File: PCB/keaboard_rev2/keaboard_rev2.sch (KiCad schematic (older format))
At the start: 80 parts, among them K01 KEYSW, K02 KEYSW, K03 KEYSW, K04 KEYSW, K05 KEYSW, K06 KEYSW, K07 KEYSW, K08 KEYSW, K09 KEYSW, K10 KEYSW, K11 KEYSW, K12 KEYSW, K13 KEYSW, K14 KEYSW, K15 KEYSW, K16 KEYSW, K17 KEYSW, K18 KEYSW, K19 KEYSW, K20 KEYSW, K21 KEYSW, K22 KEYSW, K23 KEYSW, K24 KEYSW, K25 KEYSW, U1 ProMicro

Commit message: WIP rev2
Just traces remaining
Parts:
- removed D01, D02, D03, D04, D05, D06, D07, D08, D09, D10, D11, D12, D13, D14, D15, D16, D17, D18, D19, D20, D21, D22, D23, D24, D25: D, parts:D_SOD123_reversible, symbol keyboard_parts:D
- removed K01, K02, K03, K04, K05, K06, K07, K08, K09, K10, K11, K12, K13, K14, K15, K16, K17, K18, K19, K20, K21, K22, K23, K24, K25: KEYSW, parts:Kailh_socket_MX_reversible, symbol keyboard_parts:KEYSW
- removed LED01, LED02, LED03, LED04, LED05, LED06, LED07, LED08, LED09, LED10, LED11, LED12, LED13, LED14, LED15, LED16, LED17, LED18, LED19, LED20, LED21, LED22, LED23, LED24, LED25: WS2812B, LED_SMD:LED_WS2812B_PLCC4_5.0x5.0mm_P3.2mm, symbol LED:WS2812B
- removed R01: R2.2k, symbol Device:R
- removed R02: R10k, symbol Device:R
- removed SW_RST1: SW_EVQ-9P701P, parts:SW_EVQ-9P701P_reversible, symbol Switch:SW_MEC_5G
- removed TRRS1: TRRS Jack, parts:TRRS-PJ-320A_reversible, symbol keaboard_rev2-rescue:AudioPlug4-Connector-keaboard_rev1-rescue
- added D1, D10, D11, D12, D13, D14, D15, D16, D17, D18, D19, D2, D20, D21, D22, D23, D24, D25, D3, D4, D5, D6, D7, D8, D9: 1N4148W, parts:D_SOD123_reversible, symbol Diode:1N4148W
- added J1: AudioJack4, parts:TRRS-PJ-320A_reversible, symbol Connector:AudioJack4
- added LED1, LED10, LED11, LED12, LED13, LED14, LED15, LED16, LED17, LED18, LED19, LED2, LED20, LED21, LED22, LED23, LED24, LED25, LED3, LED4, LED5, LED6, LED7, LED8, LED9: SK6812MINI, parts:YS-SK6812MINI-E_reversible, symbol LED:SK6812MINI
- added RESET1: SW_Push, parts:SW_EVQ-9P701P_reversible, symbol Switch:SW_Push
- added SW1, SW10, SW11, SW12, SW13, SW14, SW15, SW16, SW17, SW18, SW19, SW2, SW20, SW21, SW22, SW23, SW24, SW25, SW3, SW4, SW5, SW6, SW7, SW8, SW9: SW_Push, keyswitches:Kailh_socket_PG1350_reversible, symbol Switch:SW_Push
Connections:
- net GND: now also J1.S, LED1.4 (VDD), LED10.4 (VDD), LED11.4 (VDD), LED12.4 (VDD), LED13.4 (VDD), LED14.4 (VDD), LED15.4 (VDD), LED16.4 (VDD), LED17.4 (VDD), LED18.4 (VDD), LED19.4 (VDD), LED2.4 (VDD), LED20.4 (VDD), LED21.4 (VDD), LED22.4 (VDD), LED23.4 (VDD), LED24.4 (VDD), LED25.4 (VDD), LED3.4 (VDD), LED4.4 (VDD), LED5.4 (VDD), LED6.4 (VDD), LED7.4 (VDD), LED8.4 (VDD), LED9.4 (VDD), RESET1.2
- net LED: now also U1.20 (F4), LED1.3 (DIN); no longer U1.1 (TX)
- net RAW: now also LED1.2 (VSS), LED10.2 (VSS), LED11.2 (VSS), LED12.2 (VSS), LED13.2 (VSS), LED14.2 (VSS), LED15.2 (VSS), LED16.2 (VSS), LED17.2 (VSS), LED18.2 (VSS), LED19.2 (VSS), LED2.2 (VSS), LED20.2 (VSS), LED21.2 (VSS), LED22.2 (VSS), LED23.2 (VSS), LED24.2 (VSS), LED25.2 (VSS), LED3.2 (VSS), LED4.2 (VSS), LED5.2 (VSS), LED6.2 (VSS), LED7.2 (VSS), LED8.2 (VSS), LED9.2 (VSS)
- net RESET: now also RESET1.1
- net Row1: now reaches U1.8 (C6)
- net Row1: now also D1.1 (K), D13.1 (K), D17.1 (K), D21.1 (K), D5.1 (K), D9.1 (K)
- net COL1 renamed TRRS_T
- net TRRS_T: now also J1.T
- net COL2 renamed Col7
- net Col7: now also SW24.2, SW25.2
- net COL3 renamed Col6
- net Col6: now also SW21.2, SW22.2, SW23.2
- net COL4 renamed Col5
- net Col5: now also SW17.2, SW18.2, SW19.2, SW20.2
- net COL5 renamed Col4
- net Col4: now also SW13.2, SW14.2, SW15.2, SW16.2
- net COL6 renamed Col3
- net Col3: now also SW10.2, SW11.2, SW12.2, SW9.2
- net COL7 renamed Col2
- net Col2: now also SW5.2, SW6.2, SW7.2, SW8.2
- net ROW1 renamed Row2
- net Row2: now also D10.1 (K), D14.1 (K), D18.1 (K), D2.1 (K), D22.1 (K), D6.1 (K)
- net ROW2 renamed Row3
- net Row3: now also D11.1 (K), D15.1 (K), D19.1 (K), D23.1 (K), D24.1 (K), D3.1 (K), D7.1 (K)
- net ROW3 renamed Row4
- net Row4: now also D12.1 (K), D16.1 (K), D20.1 (K), D25.1 (K), D4.1 (K), D8.1 (K)
- net ROW4 renamed Col1
- net Col1: now also SW1.2, SW2.2, SW3.2, SW4.2
- net SCL renamed TRRS_R2
- net TRRS_R2: now also J1.R2
- net SDA: no longer names the net of U1.6 (SDA)
- net VCC: no longer names the net of U1.21 (VCC)
- new net: LED1.1 (DOUT), LED2.3 (DIN)
- new net: D1.2 (A), SW1.1
- new net: D5.2 (A), SW5.1
- new net: D9.2 (A), SW9.1
- new net: D13.2 (A), SW13.1
- new net: D17.2 (A), SW17.1
- new net: D21.2 (A), SW21.1
- new net: D22.2 (A), SW22.1
- new net: D18.2 (A), SW18.1
- new net: D14.2 (A), SW14.1
- new net: D10.2 (A), SW10.1
- new net: D6.2 (A), SW6.1
- new net: D2.2 (A), SW2.1
- new net: D3.2 (A), SW3.1
- new net: D7.2 (A), SW7.1
- new net: D11.2 (A), SW11.1
- new net: D15.2 (A), SW15.1
- new net: D19.2 (A), SW19.1
- new net: D23.2 (A), SW23.1
- new net: D24.2 (A), SW24.1
- new net: D25.2 (A), SW25.1
- new net: D20.2 (A), SW20.1
- new net: D16.2 (A), SW16.1
- new net: D12.2 (A), SW12.1
- new net: D8.2 (A), SW8.1
- new net: D4.2 (A), SW4.1
- new net: LED2.1 (DOUT), LED3.3 (DIN)
- new net: LED3.1 (DOUT), LED4.3 (DIN)
- new net: LED4.1 (DOUT), LED5.3 (DIN)
- new net: LED5.1 (DOUT), LED6.3 (DIN)
- new net: LED6.1 (DOUT), LED7.3 (DIN)
- new net: LED7.1 (DOUT), LED8.3 (DIN)
- new net: LED8.1 (DOUT), LED9.3 (DIN)
- new net: LED10.3 (DIN), LED9.1 (DOUT)
- new net: LED10.1 (DOUT), LED11.3 (DIN)
- new net: LED11.1 (DOUT), LED12.3 (DIN)
- new net: LED12.1 (DOUT), LED13.3 (DIN)
- new net: LED13.1 (DOUT), LED14.3 (DIN)
- new net: LED14.1 (DOUT), LED15.3 (DIN)
- new net: LED15.1 (DOUT), LED16.3 (DIN)
- new net: LED16.1 (DOUT), LED17.3 (DIN)
- new net: LED17.1 (DOUT), LED18.3 (DIN)
- new net: LED18.1 (DOUT), LED19.3 (DIN)
- new net: LED19.1 (DOUT), LED20.3 (DIN)
- new net: LED20.1 (DOUT), LED21.3 (DIN)
- new net: LED21.1 (DOUT), LED22.3 (DIN)
- new net: LED22.1 (DOUT), LED23.3 (DIN)
- new net: LED23.1 (DOUT), LED24.3 (DIN)
- new net: LED24.1 (DOUT), LED25.3 (DIN)
- no-connect marks 6 -> 7

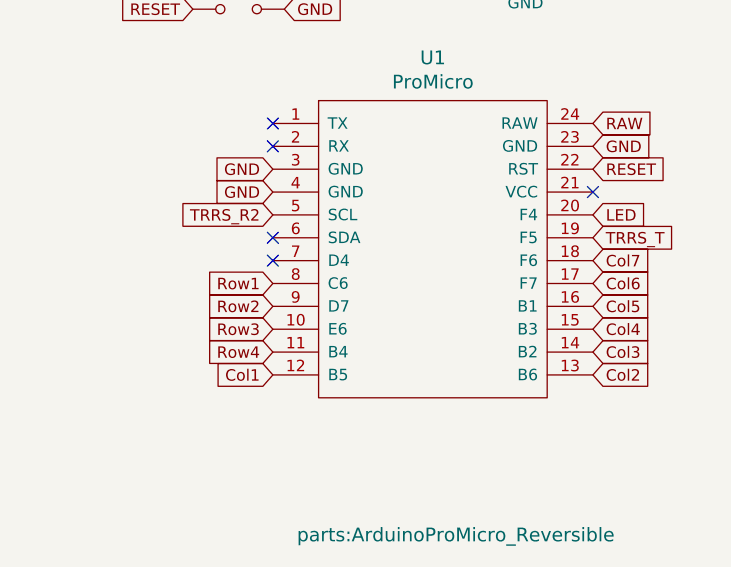
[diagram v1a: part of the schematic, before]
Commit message: Fix schematic/net mistake from old rev1 pdf
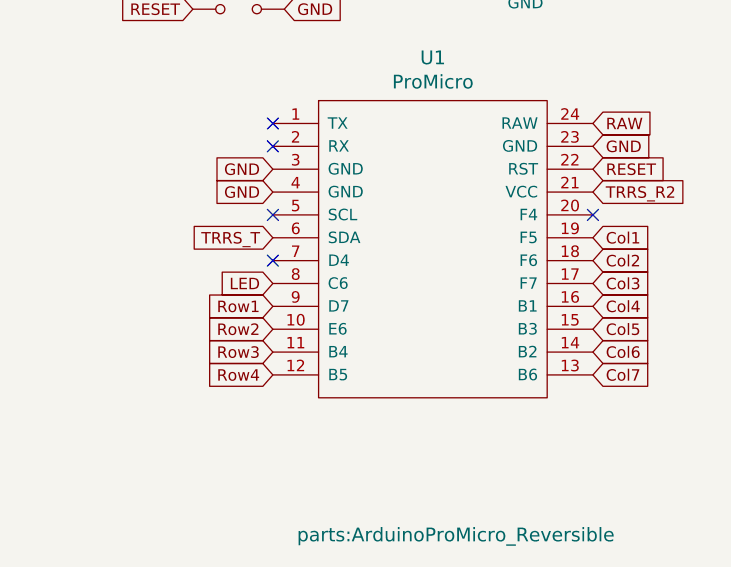
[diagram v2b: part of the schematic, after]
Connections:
- net Col1: now also U1.19 (F5); no longer U1.12 (B5)
- net Col2: now also U1.18 (F6); no longer U1.13 (B6)
- net Col3: now also U1.17 (F7); no longer U1.14 (B2)
- net Col4: now also U1.16 (B1); no longer U1.15 (B3)
- net Col5: now also U1.15 (B3); no longer U1.16 (B1)
- net Col6: now also U1.14 (B2); no longer U1.17 (F7)
- net Col7: now also U1.13 (B6); no longer U1.18 (F6)
- net LED: now also U1.8 (C6); no longer U1.20 (F4)
- net Row1: now also U1.9 (D7); no longer U1.8 (C6)
- net Row2: now also U1.10 (E6); no longer U1.9 (D7)
- net Row3: now also U1.11 (B4); no longer U1.10 (E6)
- net Row4: now also U1.12 (B5); no longer U1.11 (B4)
- net TRRS_R2: now also U1.21 (VCC); no longer U1.5 (SCL)
- net TRRS_T: now also U1.6 (SDA); no longer U1.19 (F5)
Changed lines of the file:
@@
 Text GLabel 6250 3300 1    50   Input ~ 0
 Col6
+Text GLabel 10600 5550 2    50   Input ~ 0
+Col2
+Text GLabel 10600 5650 2    50   Input ~ 0
+Col3
+Text GLabel 10600 5750 2    50   Input ~ 0
+Col4
+Text GLabel 10600 5850 2    50   Input ~ 0
+Col5
+Text GLabel 10600 5950 2    50   Input ~ 0
+Col6
+Text GLabel 9200 5750 0    50   Input ~ 0
+Row1
+Text GLabel 9200 5850 0    50   Input ~ 0
+Row2
+Text GLabel 9200 5950 0    50   Input ~ 0
+Row3
 Text GLabel 9200 6050 0    50   Input ~ 0
-Col1
-Text GLabel 10600 6050 2    50   Input ~ 0
-Col2
-Text GLabel 10600 5950 2    50   Input ~ 0
-Col3
-Text GLabel 10600 5850 2    50   Input ~ 0
-Col4
-Text GLabel 10600 5750 2    50   Input ~ 0
-Col5
-Text GLabel 10600 5650 2    50   Input ~ 0
-Col6
-Text GLabel 9200 5650 0    50   Input ~ 0
-Row1
-Text GLabel 9200 5750 0    50   Input ~ 0
-Row2
-Text GLabel 9200 5850 0    50   Input ~ 0
-Row3
-Text GLabel 9200 5950 0    50   Input ~ 0
 Row4
 Text GLabel 7150 3300 1    50   Input ~ 0
@@
 GND
 NoConn ~ 10100 3700
-Text GLabel 10600 5450 2    50   Input ~ 0
-TRRS_T
-Text GLabel 9200 5350 0    50   Input ~ 0
-TRRS_R2
 Text GLabel 10200 4250 0    50   Input ~ 0
 GND
@@
 Text GLabel 1200 1450 0    50   Input ~ 0
 RAW
-Text GLabel 10600 5350 2    50   Input ~ 0
+Text GLabel 9200 5650 0    50   Input ~ 0
 LED
-NoConn ~ 10600 5250
 NoConn ~ 9200 4950
 NoConn ~ 9200 5050
-NoConn ~ 9200 5450
 NoConn ~ 9200 5550
 Wire Wire Line
@@
 Wire Wire Line
 	6250 3300 6250 3450
-Text GLabel 10600 5550 2    50   Input ~ 0
+Text GLabel 10600 6050 2    50   Input ~ 0
 Col7
 Connection ~ 1850 1450
@@
 Wire Wire Line
 	10250 2300 10650 2300
+Text GLabel 10600 5250 2    50   Input ~ 0
+TRRS_R2
+Text GLabel 9200 5450 0    50   Input ~ 0
+TRRS_T
+Text GLabel 10600 5450 2    50   Input ~ 0
+Col1
+NoConn ~ 10600 5350
+NoConn ~ 9200 5350
 $EndSCHEMATC

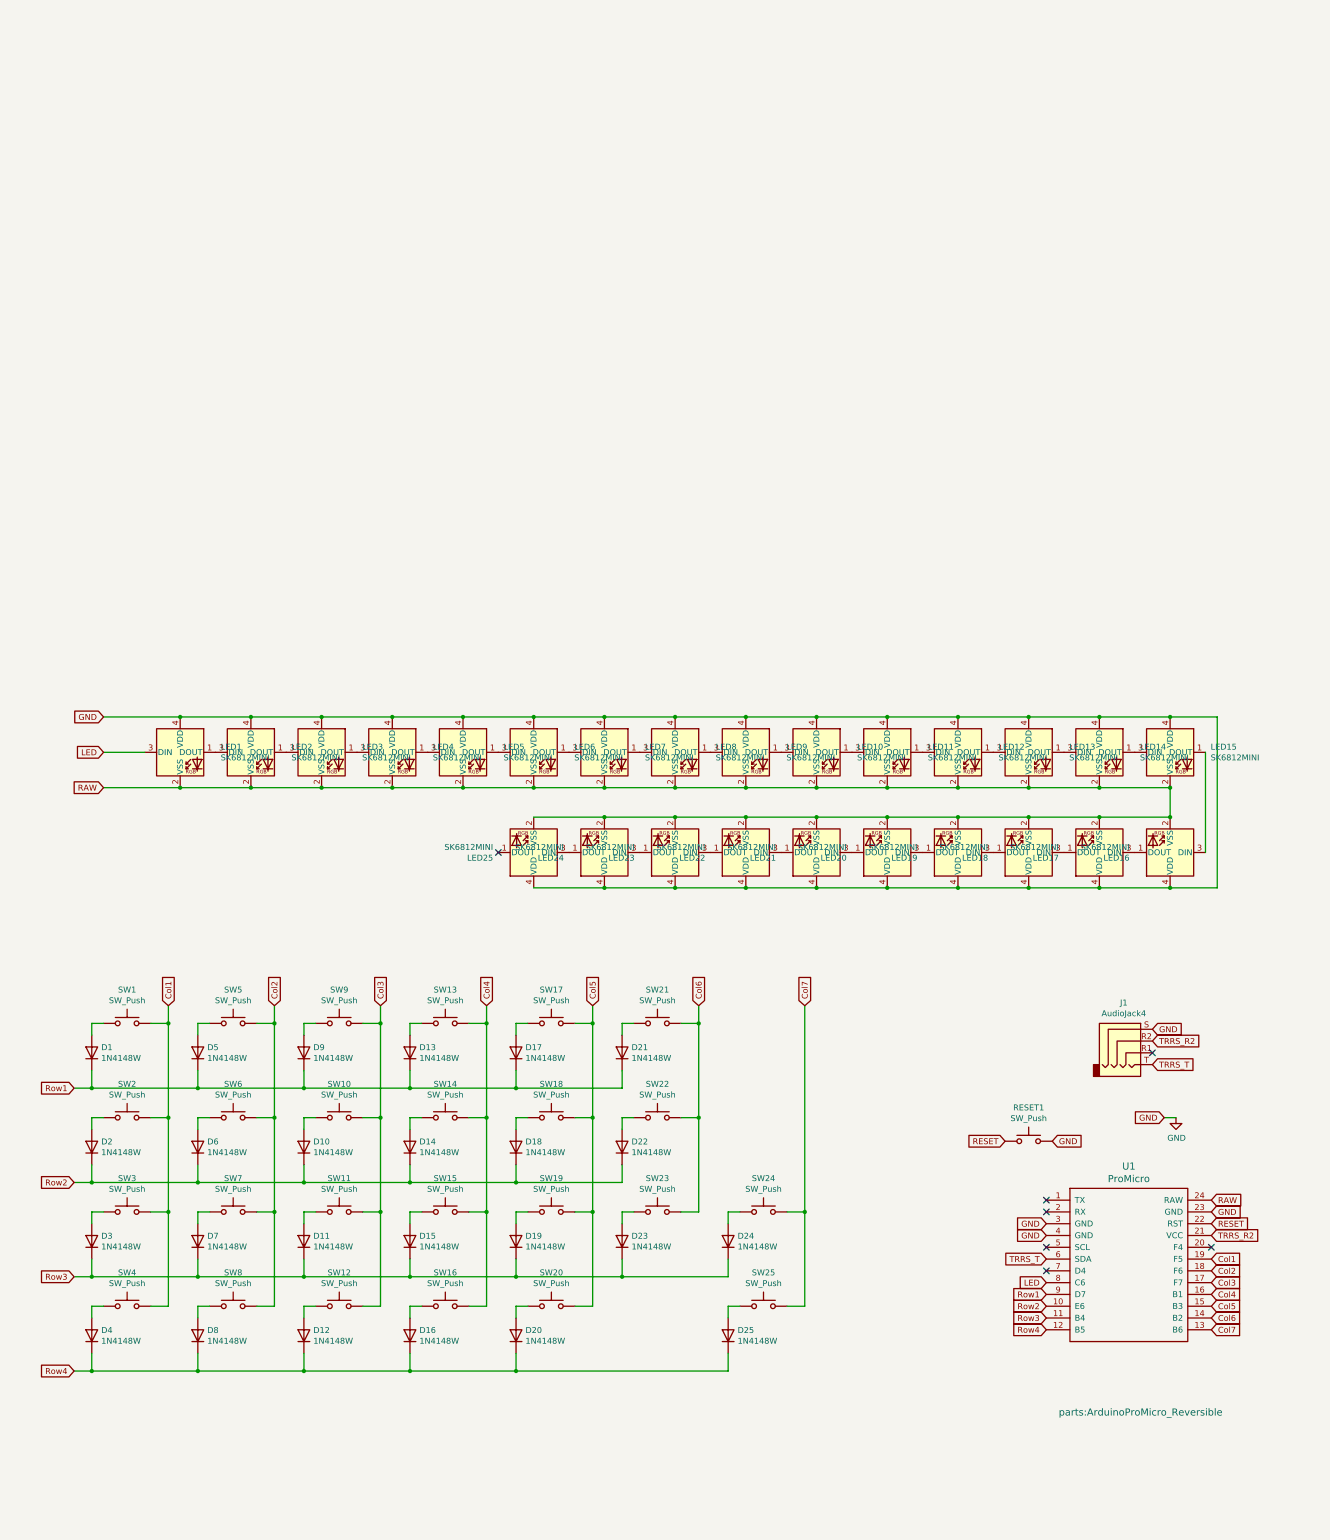
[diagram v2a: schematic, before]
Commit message: Reorder LEDs in schematic for better routing
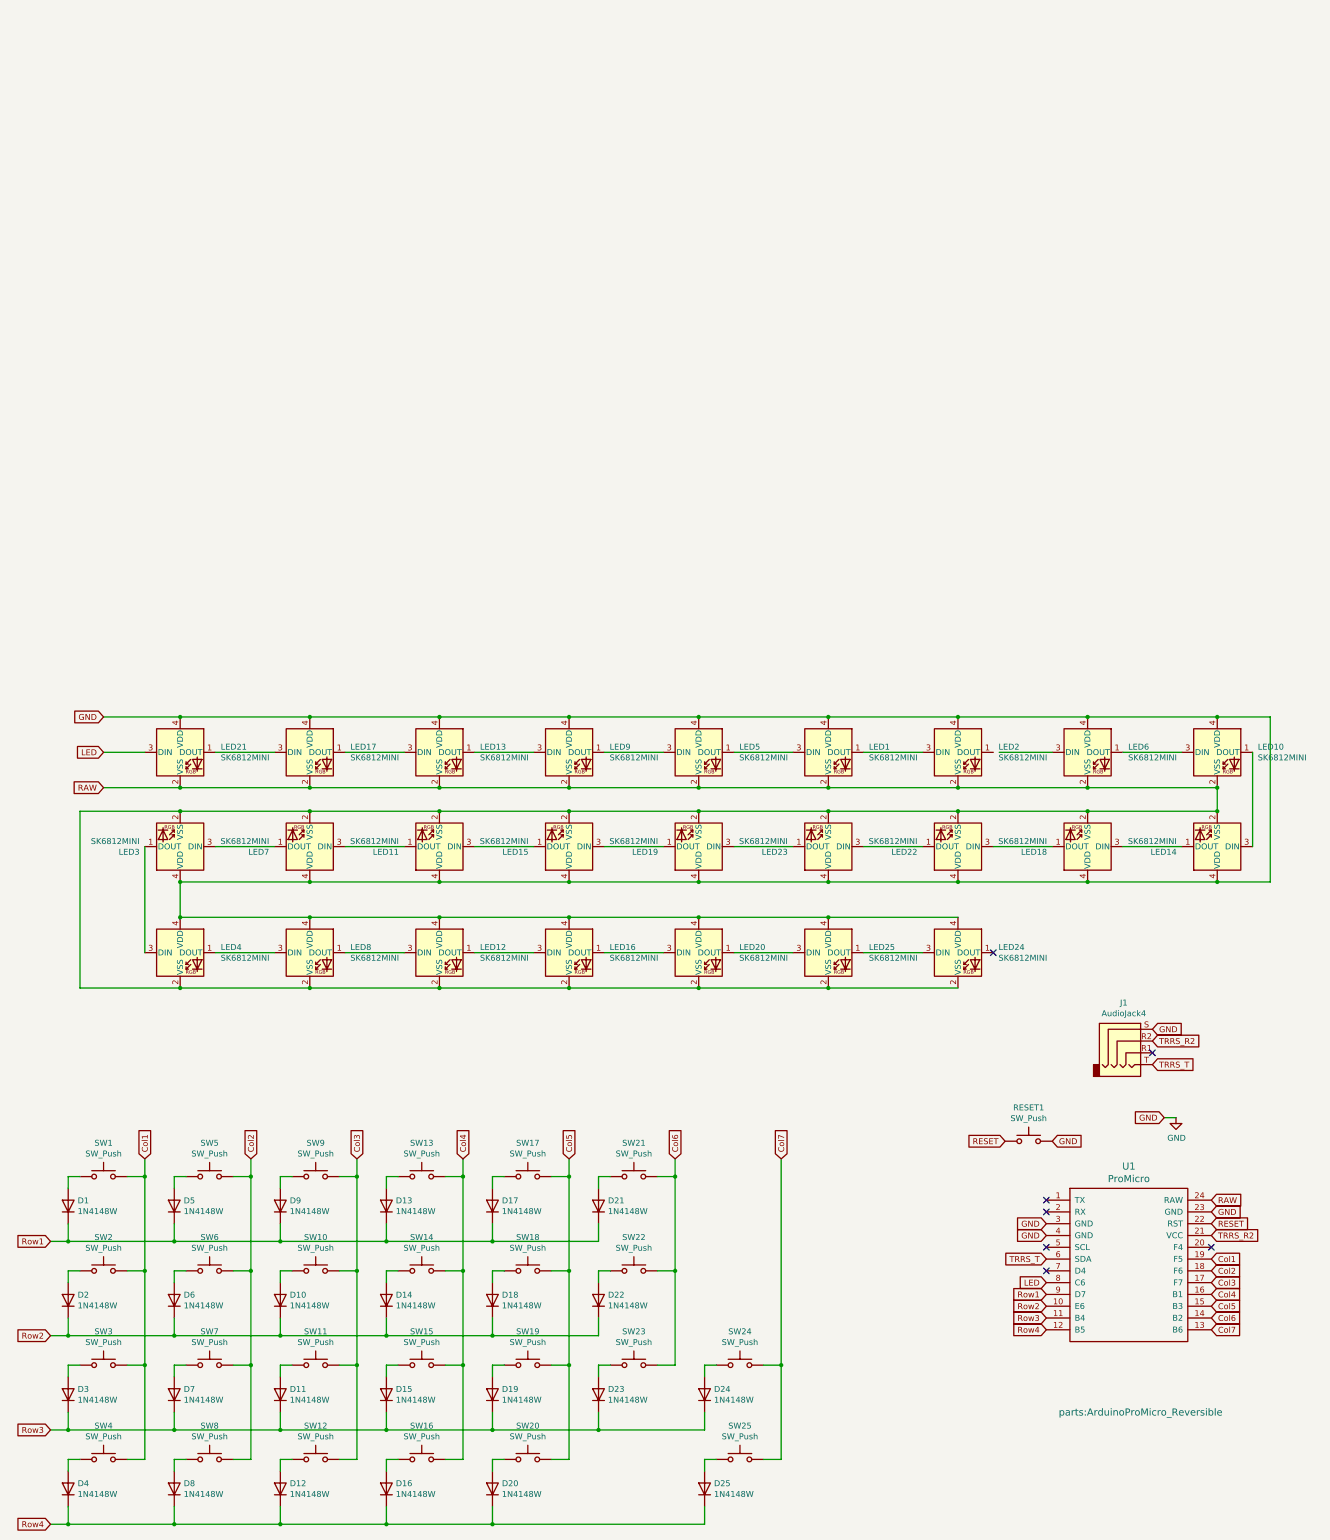
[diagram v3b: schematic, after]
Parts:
- removed LED21: SK6812MINI, parts:YS-SK6812MINI-E_reversible, symbol LED:SK6812MINI
- added LED1: SK6812MINI, parts:YS-SK6812MINI-E_reversible, symbol LED:SK6812MINI
- renumbered LED1 to LED21
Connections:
- net GND: now also LED1.4 (VDD)
- net RAW: now also LED1.2 (VSS)
- net at LED21.1 (DOUT): now also LED17.3 (DIN); no longer LED2.3 (DIN)
- net at LED2.1 (DOUT): no longer LED3.3 (DIN)
- net at LED5.3 (DIN): now also LED9.1 (DOUT); no longer LED4.1 (DOUT)
- net at LED5.1 (DOUT): now also LED1.3 (DIN); no longer LED6.3 (DIN)
- net at LED6.1 (DOUT): now also LED10.3 (DIN); no longer LED7.3 (DIN)
- net at LED7.1 (DOUT): now also LED3.3 (DIN); no longer LED8.3 (DIN)
- net at LED9.3 (DIN): now also LED13.1 (DOUT); no longer LED8.1 (DOUT)
- net at LED10.1 (DOUT): now also LED14.3 (DIN); no longer LED11.3 (DIN)
- net at LED11.1 (DOUT): now also LED7.3 (DIN); no longer LED12.3 (DIN)
- net at LED13.3 (DIN): now also LED17.1 (DOUT); no longer LED12.1 (DOUT)
- net at LED14.1 (DOUT): now also LED18.3 (DIN); no longer LED15.3 (DIN)
- net at LED15.1 (DOUT): now also LED11.3 (DIN); no longer LED16.3 (DIN)
- net at LED16.1 (DOUT): now also LED20.3 (DIN); no longer LED17.3 (DIN)
- net at LED18.1 (DOUT): now also LED22.3 (DIN); no longer LED19.3 (DIN)
- net at LED19.1 (DOUT): now also LED15.3 (DIN); no longer LED20.3 (DIN)
- net at LED20.1 (DOUT): now also LED25.3 (DIN)
- net at LED23.1 (DOUT): now also LED19.3 (DIN); no longer LED24.3 (DIN)
- net at LED24.1 (DOUT): no longer LED25.3 (DIN)
- net at LED25.1 (DOUT): now also LED24.3 (DIN)
- new net: LED1.1 (DOUT), LED2.3 (DIN)
- new net: LED4.1 (DOUT), LED8.3 (DIN)
- new net: LED12.3 (DIN), LED8.1 (DOUT)
- new net: LED12.1 (DOUT), LED16.3 (DIN)
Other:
- moved on the sheet: D1, D10, D11, D12, D13, D14, D15, D16, D17, D18, D19, D2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
